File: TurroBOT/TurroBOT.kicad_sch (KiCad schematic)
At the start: 12 parts, among them J3 Conn_01x10_Pin, J4 Motor2, J5 molex macho 2P, J6 Motor2, SW1 SW_Push, SW2 SW_SPDT, U1 YAAJ_DCDC_StepUp_SX1308, U2 ROB-14450

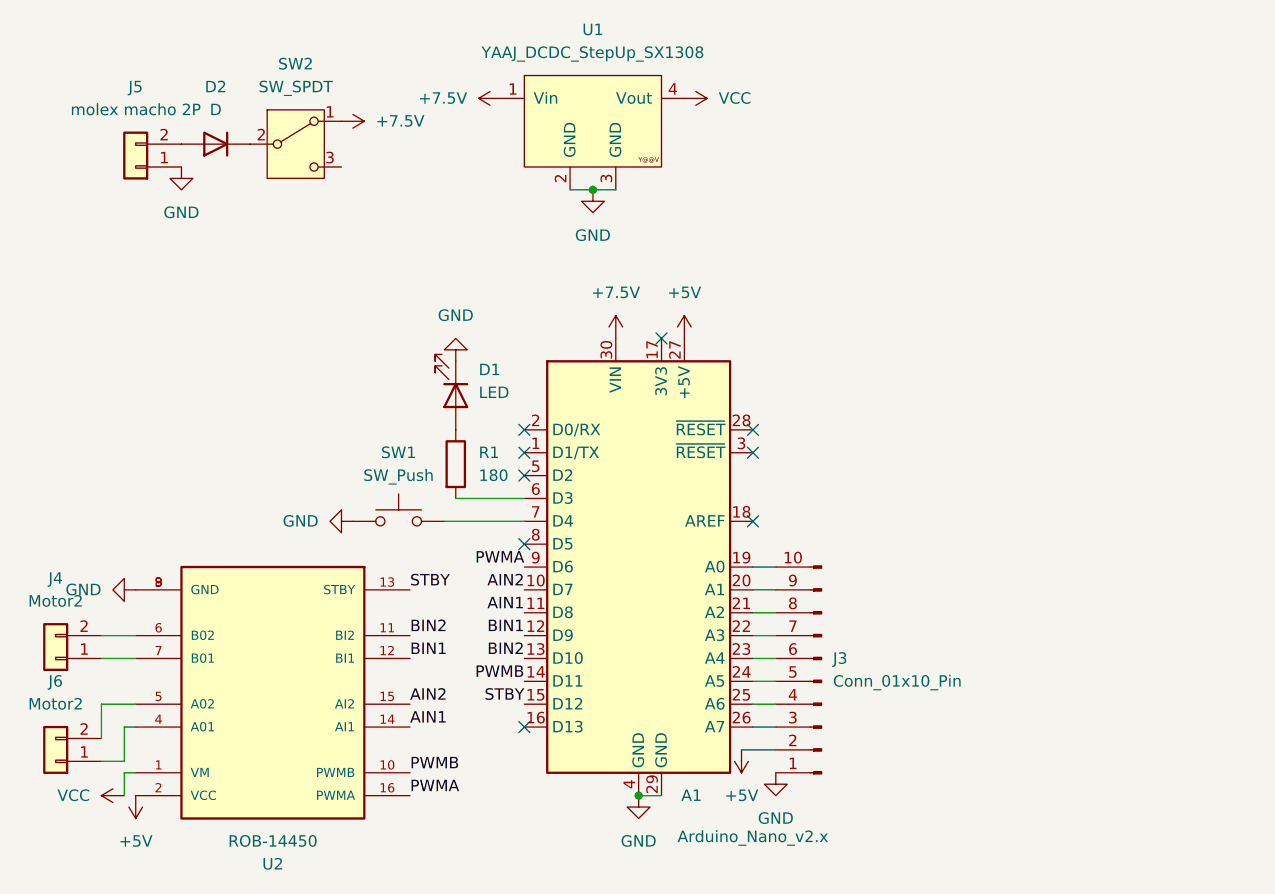
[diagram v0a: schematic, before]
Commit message: casi todas las footprints cargadas
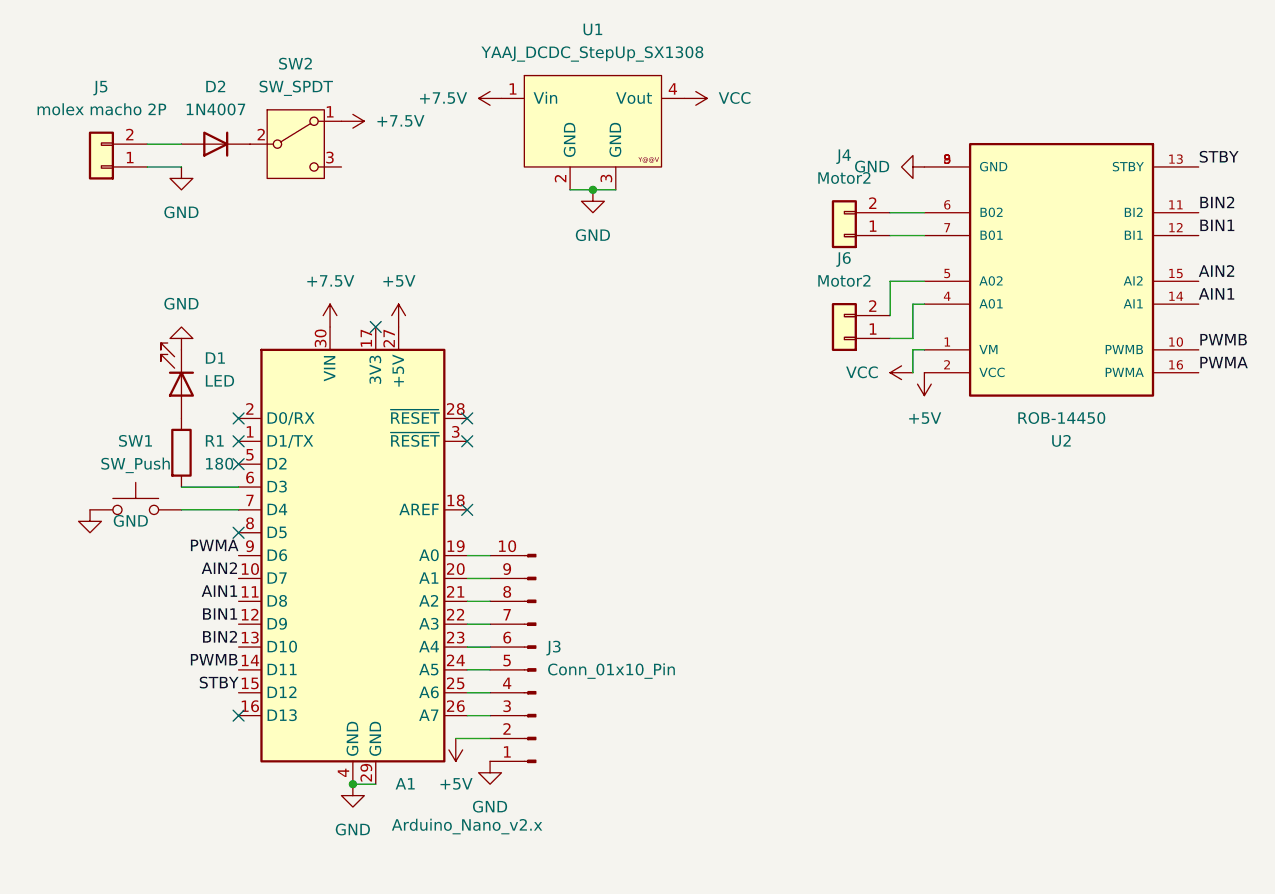
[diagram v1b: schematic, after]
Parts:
- D2: value D -> 1N4007
- J3: footprint (none) -> Connector_PinHeader_2.00mm:PinHeader_1x10_P2.00mm_Vertical
- SW1: footprint (none) -> Button_Switch_THT:SW_PUSH_6mm
- U1: footprint (none) -> KiCad:YAAJ_DCDC_StepUp_SX1308
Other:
- moved on the sheet: A1, D1, J3, J4, J5, J6, R1, SW1, U2

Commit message: falta solo footprint del switch
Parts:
- D1: footprint (none) -> LED_THT:LED_D3.0mm
- D2: footprint (none) -> Diode_THT:D_DO-41_SOD81_P10.16mm_Horizontal
- J4, J5, J6: footprint Molex:Molex_01x02 -> Connector_Molex:Molex_KK-254_AE-6410-02A_1x02_P2.54mm_Vertical
- R1: footprint (none) -> Resistor_SMD:R_1206_3216Metric
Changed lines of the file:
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@@
 			)
 		)
-		(property "Footprint" ""
+		(property "Footprint" "Diode_THT:D_DO-41_SOD81_P10.16mm_Horizontal"
 			(at 38.1 41.91 0)
 			(effects
@@
 			)
 		)
-		(property "Footprint" ""
+		(property "Footprint" "Resistor_SMD:R_1206_3216Metric"
 			(at 32.512 76.2 90)
 			(effects
@@
 			)
 		)
-		(property "Footprint" "Molex:Molex_01x02"
+		(property "Footprint" "Connector_Molex:Molex_KK-254_AE-6410-02A_1x02_P2.54mm_Vertical"
 			(at 25.4 44.45 0)
 			(effects
@@
 			)
 		)
-		(property "Footprint" ""
+		(property "Footprint" "LED_THT:LED_D3.0mm"
 			(at 34.29 68.58 0)
 			(effects
@@
 			)
 		)
-		(property "Footprint" "Molex:Molex_01x02"
+		(property "Footprint" "Connector_Molex:Molex_KK-254_AE-6410-02A_1x02_P2.54mm_Vertical"
 			(at 107.95 52.07 0)
 			(effects
@@
 			)
 		)
-		(property "Footprint" "Molex:Molex_01x02"
+		(property "Footprint" "Connector_Molex:Molex_KK-254_AE-6410-02A_1x02_P2.54mm_Vertical"
 			(at 107.95 63.5 0)
 			(effects

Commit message: todo listo
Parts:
- SW2: footprint Switch:SW_9mm -> Button_Switch_THT:SW_Slide_SPDT_Straight_CK_OS102011MS2Q
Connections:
- net at R1.2: now also A1.16 (D13); no longer A1.6 (D3)
- no-connect marks 9 -> 8
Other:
- moved on the sheet: D1, R1, SW1
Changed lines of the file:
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@@
+		(color 0 0 0 0)
+	)
+	(junction
+		(at 25.4 80.01)
+		(diameter 0)
 		(color 0 0 0 0)
 	)
@@
 	)
 	(no_connect
-		(at 40.64 105.41)
-	)
-	(no_connect
 		(at 40.64 85.09)
 	)
@@
 	(wire
 		(pts
-			(xy 34.29 82.55) (xy 40.64 82.55)
+			(xy 29.21 105.41) (xy 40.64 105.41)
 		)
 		(stroke
@@
 	(wire
 		(pts
-			(xy 34.29 80.01) (xy 40.64 80.01)
+			(xy 25.4 80.01) (xy 25.4 81.28)
 		)
 		(stroke
@@
 	(wire
 		(pts
+			(xy 35.56 80.01) (xy 35.56 82.55)
+		)
+		(stroke
+			(width 0)
+			(type default)
+		)
+	)
+	(wire
+		(pts
 			(xy 116.84 49.53) (xy 113.03 49.53)
+		)
+		(stroke
+			(width 0)
+			(type default)
+		)
+	)
+	(wire
+		(pts
+			(xy 35.56 82.55) (xy 40.64 82.55)
 		)
 		(stroke
@@
 			)
 		)
-		(property "Footprint" "Switch:SW_9mm"
+		(property "Footprint" "Button_Switch_THT:SW_Slide_SPDT_Straight_CK_OS102011MS2Q"
 			(at 46.99 41.91 0)
 			(effects
@@
 	(symbol
 		(lib_id "Device:R")
-		(at 34.29 76.2 0)
+		(at 29.21 101.6 0)
 		(unit 1)
 		(exclude_from_sim no)
@@
 		(fields_autoplaced yes)
 		(property "Reference" "R1"
-			(at 36.83 74.9299 0)
+			(at 31.75 100.3299 0)
 			(effects
 				(font
@@
 		)
 		(property "Value" "180"
-			(at 36.83 77.4699 0)
+			(at 31.75 102.8699 0)
 			(effects
 				(font
@@
 		)
 		(property "Footprint" "Resistor_SMD:R_1206_3216Metric"
-			(at 32.512 76.2 90)
+			(at 27.432 101.6 90)
 			(effects
 				(font
@@
 		)
 		(property "Datasheet" "~"
-			(at 34.29 76.2 0)
+			(at 29.21 101.6 0)
 			(effects
 				(font
@@
 		)
 		(property "Description" "Resistor"
-			(at 34.29 76.2 0)
+			(at 29.21 101.6 0)
 			(effects
 				(font
@@
 	(symbol
 		(lib_id "Switch:SW_Push")
-		(at 29.21 82.55 0)
+		(at 30.48 80.01 0)
 		(unit 1)
 		(exclude_from_sim no)
@@
 		(fields_autoplaced yes)
 		(property "Reference" "SW1"
-			(at 29.21 74.93 0)
+			(at 30.48 72.39 0)
 			(effects
 				(font
@@
 		)
 		(property "Value" "SW_Push"
-			(at 29.21 77.47 0)
+			(at 30.48 74.93 0)
 			(effects
 				(font
@@
 		)
 		(property "Footprint" "Button_Switch_THT:SW_PUSH_6mm"
-			(at 29.21 77.47 0)
+			(at 30.48 74.93 0)
 			(effects
 				(font
@@
 		)
 		(property "Datasheet" "~"
-			(at 29.21 77.47 0)
+			(at 30.48 74.93 0)
 			(effects
 				(font
@@
 		)
 		(property "Description" "Push button switch, generic, two pins"
-			(at 29.21 82.55 0)
+			(at 30.48 80.01 0)
 			(effects
 				(font
@@
 	(symbol
 		(lib_id "power:GND")
-		(at 24.13 82.55 0)
-		(unit 1)
-		(exclude_from_sim no)
-		(in_bom yes)
-		(on_board yes)
-		(dnp no)
-		(fields_autoplaced yes)
+		(at 25.4 80.01 0)
+		(unit 1)
+		(exclude_from_sim no)
+		(in_bom yes)
+		(on_board yes)
+		(dnp no)
 		(property "Reference" "#PWR011"
-			(at 24.13 88.9 0)
+			(at 25.4 86.36 0)
 			(effects
 				(font
@@
 		)
 		(property "Value" "GND"
-			(at 26.67 83.8199 0)
+			(at 23.368 84.074 0)
 			(effects
 				(font
@@
 		)
 		(property "Footprint" ""
-			(at 24.13 82.55 0)
+			(at 25.4 80.01 0)
 			(effects
 				(font
@@
 		)
 		(property "Datasheet" ""
-			(at 24.13 82.55 0)
+			(at 25.4 80.01 0)
 			(effects
 				(font
@@
 		)
 		(property "Description" "Power symbol creates a global label with name \"GND\" , ground"
-			(at 24.13 82.55 0)
+			(at 25.4 80.01 0)
 			(effects
 				(font
@@
 	(symbol
 		(lib_id "power:GND")
-		(at 34.29 64.77 180)
+		(at 29.21 90.17 180)
 		(unit 1)
 		(exclude_from_sim no)
@@
 		(fields_autoplaced yes)
 		(property "Reference" "#PWR06"
-			(at 34.29 58.42 0)
+			(at 29.21 83.82 0)
 			(effects
 				(font
@@
 		)
 		(property "Value" "GND"
-			(at 34.29 59.69 0)
+			(at 29.21 85.09 0)
 			(effects
 				(font
@@
 		)
 		(property "Footprint" ""
-			(at 34.29 64.77 0)
+			(at 29.21 90.17 0)
 			(effects
 				(font
@@
 		)
 		(property "Datasheet" ""
-			(at 34.29 64.77 0)
+			(at 29.21 90.17 0)
 			(effects
 				(font
@@
 		)
 		(property "Description" "Power symbol creates a global label with name \"GND\" , ground"
-			(at 34.29 64.77 0)
+			(at 29.21 90.17 0)
 			(effects
 				(font
@@
 	(symbol
 		(lib_id "Device:LED")
-		(at 34.29 68.58 270)
+		(at 29.21 93.98 270)
 		(unit 1)
 		(exclude_from_sim no)
@@
 		(fields_autoplaced yes)
 		(property "Reference" "D1"
-			(at 36.83 65.7224 90)
+			(at 31.75 91.1224 90)
 			(effects
 				(font
@@
 		)
 		(property "Value" "LED"
-			(at 36.83 68.2624 90)
+			(at 31.75 93.6624 90)
 			(effects
 				(font
@@
 		)
 		(property "Footprint" "LED_THT:LED_D3.0mm"
-			(at 34.29 68.58 0)
+			(at 29.21 93.98 0)
 			(effects
 				(font
@@
 		)
 		(property "Datasheet" "~"
-			(at 34.29 68.58 0)
+			(at 29.21 93.98 0)
 			(effects
 				(font
@@
 		)
 		(property "Description" "Light emitting diode"
-			(at 34.29 68.58 0)
-			(effects
-				(font
+			(at 29.21 93.98 0)
+			(effects
+				(font
